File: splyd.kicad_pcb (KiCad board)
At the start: 2 copper layers, 324.2 x 209.9 mm, 272 parts

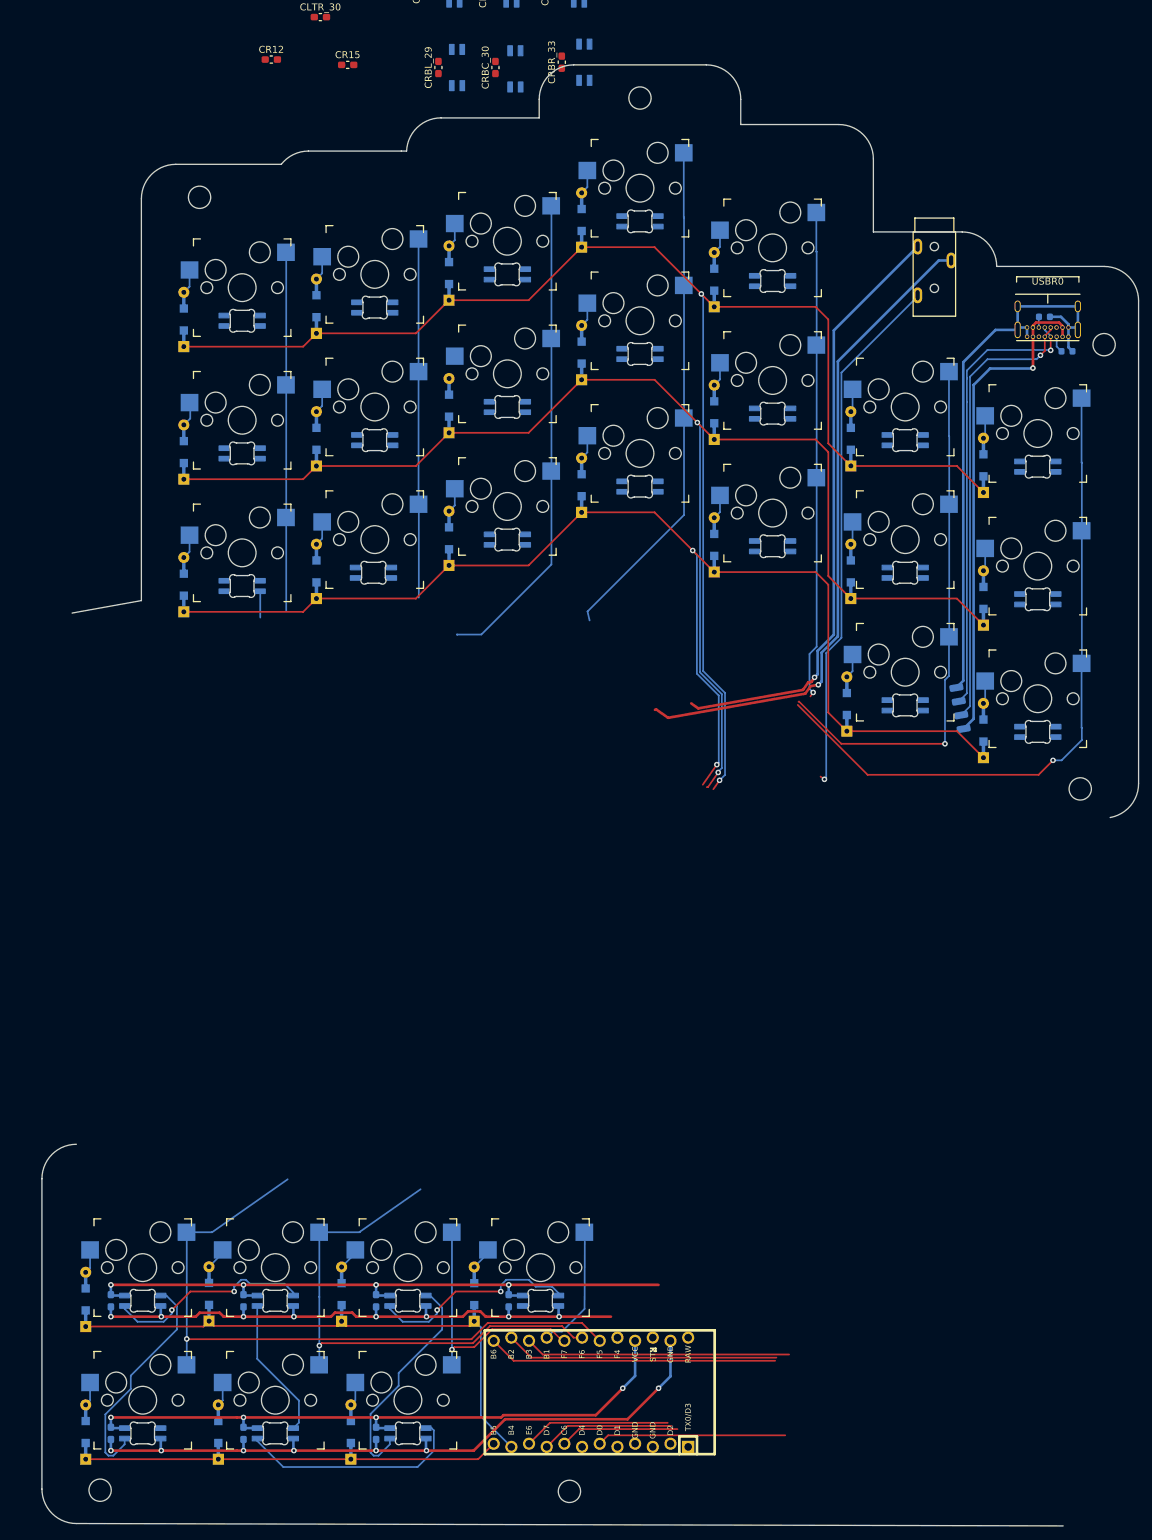
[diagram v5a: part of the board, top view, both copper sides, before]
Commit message: Wire bottom left underglow LED on right hand
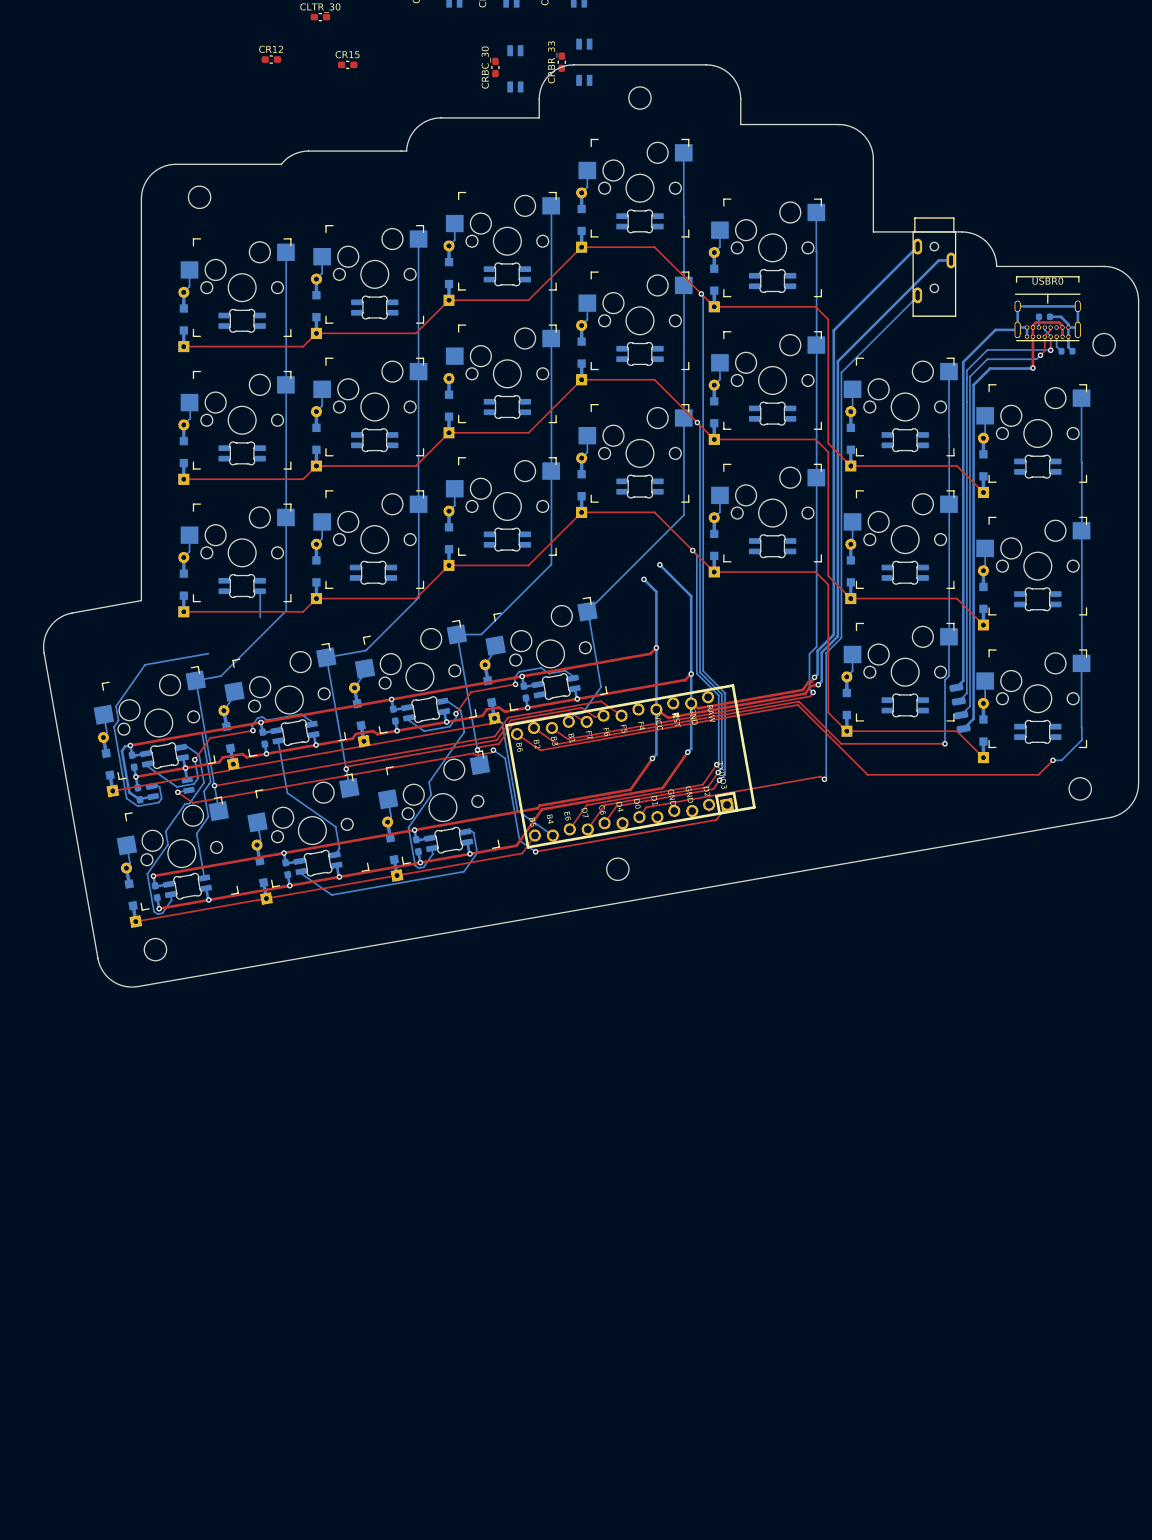
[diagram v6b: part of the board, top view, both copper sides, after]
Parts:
- removed the REF** at (266.1, 254.8)
- removed the REF** at (198.7, 254.6)
- added REF**: MountingHole_3.2mm_M3_edge_distance, Mounting_Wuerth:MountingHole_3.2mm_M3_edge_distance, B.Cu at (273.1, 165.4)
- added REF**: MountingHole_3.2mm_M3_edge_distance, Mounting_Wuerth:MountingHole_3.2mm_M3_edge_distance, B.Cu at (206.6, 177.0)
- CRBL_29: moved to B.Cu
- moved CRBL_29 112.9 mm to (204.3, 154.6), turned to 100 degrees
- moved DRBL_29 111.4 mm to (208.8, 153.8), turned to 100 degrees
- moved UR0 89.8 mm to (273.6, 150.9), turned to 190 degrees
- moved DR33_28 88.3 mm to (264.2, 139.2), turned to 280 degrees
- moved KR33 88.2 mm to (263.4, 134.5), turned to 10 degrees
- moved CR33 87.5 mm to (259.7, 140.0), turned to 280 degrees
- moved DR33 86.6 mm to (254.7, 139.9), turned to 100 degrees
- moved DR42_26 85.4 mm to (248.8, 161.3), turned to 280 degrees
- moved KR42 85.3 mm to (247.9, 156.6), turned to 10 degrees
- moved DR32_27 85.0 mm to (245.5, 142.5), turned to 280 degrees
- moved KR32 84.9 mm to (244.6, 137.8), turned to 10 degrees
- moved CR42 84.6 mm to (244.3, 162.1), turned to 280 degrees
- moved CR32 84.2 mm to (241.0, 143.3), turned to 280 degrees
- moved DR42 84.0 mm to (240.7, 162.5), turned to 100 degrees
- moved DR32 83.3 mm to (235.9, 143.2), turned to 100 degrees
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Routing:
- net RLED: track 0.00 -> 94.3 mm, vias 0 -> 3
- net Net-(DRBL_29-Pad2): track 0.00 -> 38.8 mm
- net GND2: track 272.4 -> 306.7 mm, vias 16 -> 18
- net R5V: track 283.9 -> 313.0 mm, vias 9 -> 11
- net Net-(DR20_21-Pad2): track 0.34 -> 21.9 mm
- net Net-(DR30_23-Pad2): track 30.0 -> 32.5 mm
- net Net-(DR31_24-Pad2): track 21.1 -> 20.4 mm
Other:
- board size 324.2 x 209.9 mm -> 324.2 x 132.5 mm

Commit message: Place all RGB LEDs
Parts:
- CL33, CL34, CL35, CL36, CL45, CL46, CLBC_32, CLBR_29, CR15, CRBC_30, CRBR_33: moved to B.Cu
- moved CL44 177.1 mm to (125.0, 179.2)
- moved CLBL_33 165.3 mm to (42.3, 153.9)
- moved CL20 165.2 mm to (33.0, 143.0)
- moved CL21 161.5 mm to (53.4, 138.5)
- moved CL46 159.1 mm to (164.0, 182.5), turned to 270 degrees
- moved CL11 157.5 mm to (52.0, 120.2)
- moved CL33 154.5 mm to (106.5, 164.0), turned to 270 degrees
- moved CL01 153.8 mm to (53.6, 100.9)
- moved CR26 153.2 mm to (329.0, 143.4)
- moved CL45 147.1 mm to (145.0, 182.5), turned to 270 degrees
- moved CR25 143.2 mm to (309.6, 138.7)
- moved CR06 139.3 mm to (329.6, 104.8)
- moved CL10 137.8 mm to (33.6, 124.4)
- moved CL35 136.9 mm to (145.4, 163.6), turned to 90 degrees
- moved CLBR_29 135.8 mm to (164.0, 168.2), turned to 90 degrees
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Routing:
- net Net-(KR06-Pad1): track 138.0 -> 103.3 mm, vias 1 -> 0
- net Net-(DR20_21-Pad2): track 21.9 -> 47.6 mm
- net Net-(KL03-Pad1): track 109.4 -> 90.5 mm
- net GND2: track 306.7 -> 312.7 mm, vias 18 -> 19
- net Net-(DL33-Pad1): track 59.5 -> 57.6 mm
- net Net-(DL44-Pad1): track 55.7 -> 57.0 mm
- net R5V: track 313.0 -> 313.8 mm, vias 11 -> 12
- net Net-(DR26-Pad2): track 3.32 -> 2.74 mm
- net Net-(KL05-Pad1): track 139.7 -> 139.3 mm, vias 1 -> 2
- net Net-(KL04-Pad1): track 124.0 -> 124.1 mm, vias 1 -> 2
- net Net-(KL06-Pad1): vias 1 -> 2
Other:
- board size 324.2 x 132.5 mm -> 324.2 x 145.9 mm

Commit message: Wire all LEDs on left thumb cluster
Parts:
- added R_LLED1: 500, Resistor_SMD:R_0603_1608Metric, B.Cu at (154.0, 153.3)
- added R_RLED1: 500, Resistor_SMD:R_0603_1608Metric, B.Cu at (218.4, 153.8)
- CL44: moved to B.Cu
- moved CLBC_32 28.0 mm to (87.3, 137.6), turned to 80 degrees
- moved DLBC_32 27.2 mm to (91.8, 138.4), turned to 80 degrees
- moved REF** 26.8 mm to (98.5, 165.4), turned to 0 degrees
- moved UL0 26.4 mm to (97.9, 150.9), turned to 350 degrees
- moved DL33 25.9 mm to (99.2, 136.8), turned to 80 degrees
- moved CL33 25.8 mm to (102.8, 138.4), turned to 260 degrees
- moved DL33_28 25.1 mm to (107.3, 139.2), turned to 260 degrees
- moved KL33 24.4 mm to (108.1, 134.5), turned to 350 degrees
- moved DL44 23.9 mm to (114.5, 159.7), turned to 80 degrees
- moved DL44_26 23.3 mm to (122.8, 161.3), turned to 260 degrees
- moved DL34 22.7 mm to (117.9, 140.9), turned to 80 degrees
- moved CL34 22.6 mm to (121.6, 141.7), turned to 260 degrees
- moved KL44 22.2 mm to (123.6, 156.6), turned to 350 degrees
- moved DL34_27 21.9 mm to (126.1, 142.5), turned to 260 degrees
- moved KL34 21.2 mm to (126.9, 137.8), turned to 350 degrees
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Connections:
- UL0 pad 1: LLED -> Net-(R_LLED1-Pad2)
- UR0 pad 1: RLED -> Net-(R_RLED1-Pad1)
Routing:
- net GND1: track 104.6 -> 326.0 mm, vias 1 -> 18
- net L5V: track 102.3 -> 318.9 mm, vias 1 -> 12
- net RLED: track 94.3 -> 8.09 mm, vias 3 -> 2
- net Net-(R_RLED1-Pad1): track 0.00 -> 82.9 mm, vias 0 -> 3
- net Net-(R_LLED1-Pad2): track 0.00 -> 74.5 mm, vias 0 -> 2
- net Net-(DL26_21-Pad2): track 0.00 -> 43.2 mm
- net Net-(DLBR_29-Pad2): track 0.00 -> 28.5 mm
- net Net-(DL36_23-Pad4): track 0.00 -> 27.8 mm
- net Net-(DL34_27-Pad4): track 0.00 -> 27.4 mm
- net Net-(DL35_24-Pad2): track 0.00 -> 19.7 mm
- net Net-(KL03-Pad1): track 90.5 -> 109.4 mm
- net Net-(DL35_24-Pad4): track 0.00 -> 14.5 mm, vias 0 -> 2
- net Net-(DL44_26-Pad4): track 0.00 -> 14.5 mm
- net Net-(DL33_28-Pad4): track 0.00 -> 14.5 mm, vias 0 -> 2
- net LLED: track 0.00 -> 11.3 mm
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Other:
- board size 324.2 x 145.9 mm -> 324.2 x 132.5 mm
